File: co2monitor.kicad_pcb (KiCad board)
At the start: 2 copper layers, 70 x 70 mm, 37 parts, among them J1 USB_C_Receptacle_USB2.0, J2 UART, SW1 RESET, SW2 BOOT, U1 AP2112K-3.3, U2 ESP32-S3-WROOM-1, U3 BME680, U4 SCD40, U5 74AHCT1G125, U6 SHT30-DIS

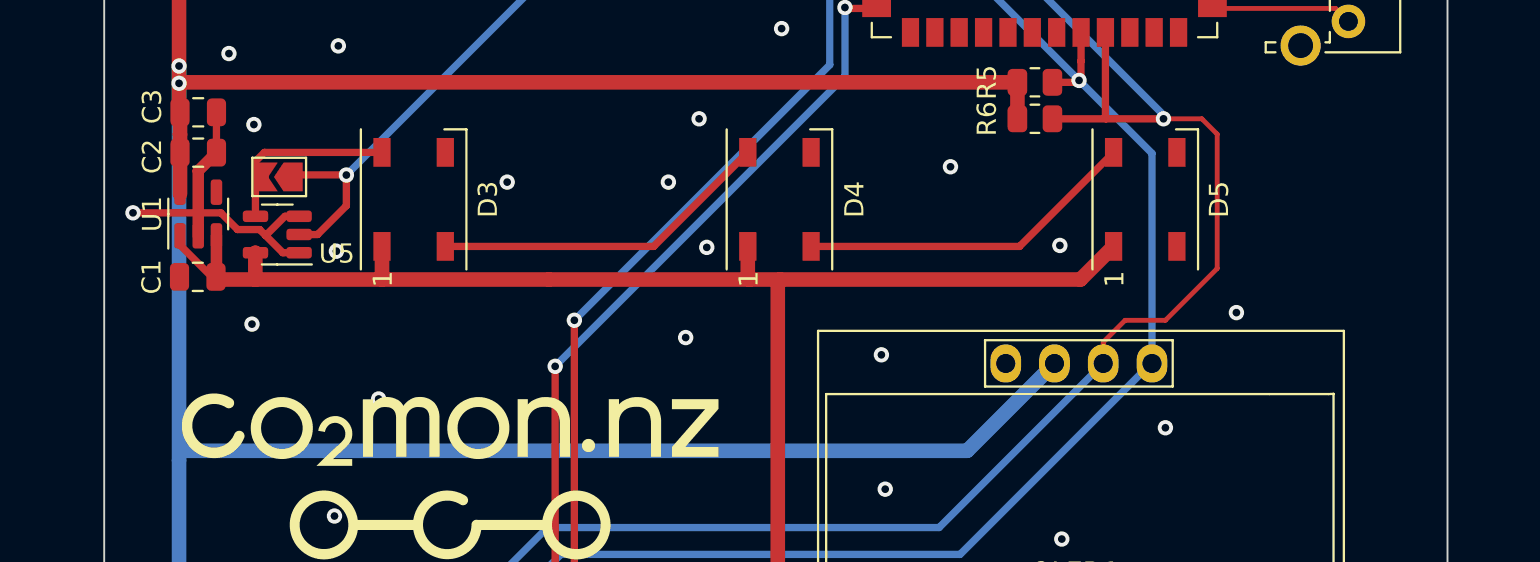
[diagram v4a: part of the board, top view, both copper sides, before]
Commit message: Break out various signals to debugging headers
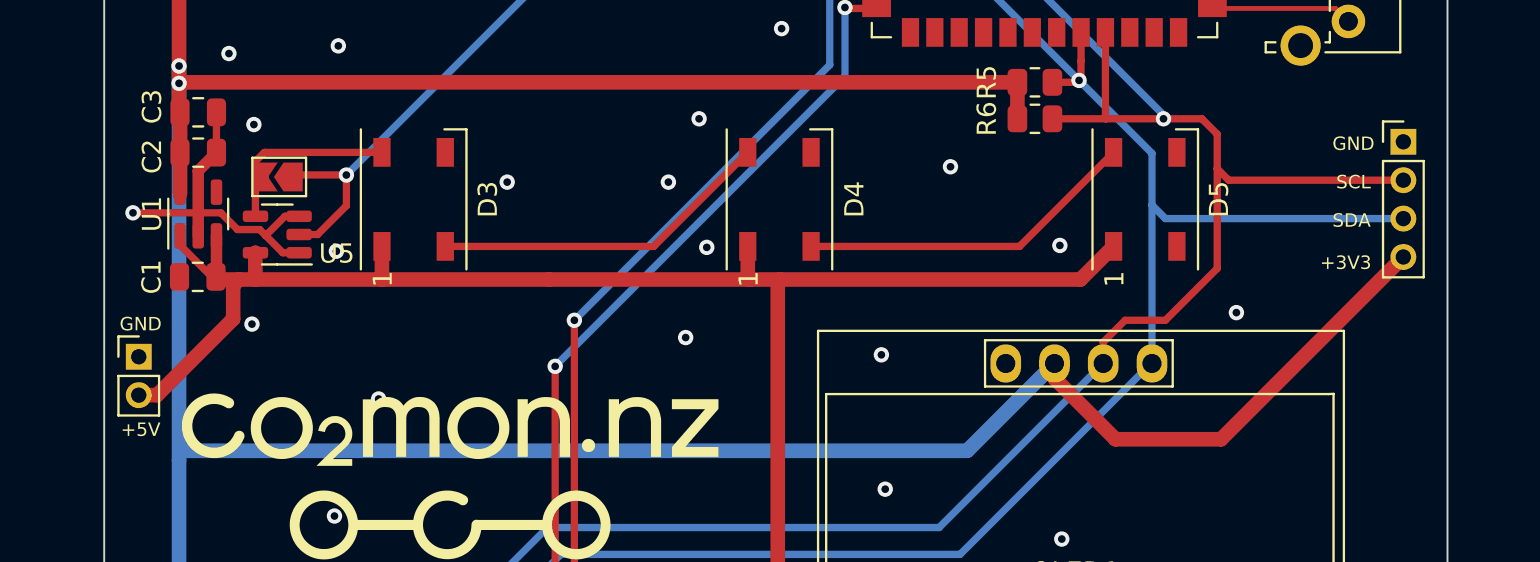
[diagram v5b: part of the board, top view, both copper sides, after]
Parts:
- added J3: I2C, Connector_PinHeader_2.00mm:PinHeader_1x04_P2.00mm_Vertical, F.Cu at (167.7, 102.0)
- added J4: 5V, Connector_PinHeader_2.00mm:PinHeader_1x02_P2.00mm_Vertical, F.Cu at (101.8, 113.2)
- D3, D4, D5: value NeoPixel_THT -> WS2812B
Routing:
- net +3V3: track 226.5 -> 250.7 mm
- net /SDA: track 130.0 -> 143.4 mm
- net /SCL: track 142.1 -> 152.1 mm
- net +5V: track 74.1 -> 82.8 mm
- net GND: vias 35 -> 34
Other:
- board text added: "+3V3"
- board text added: "+5V"
- board text added: "GND"
- board text added: "SCL"
- board text added: "SDA"

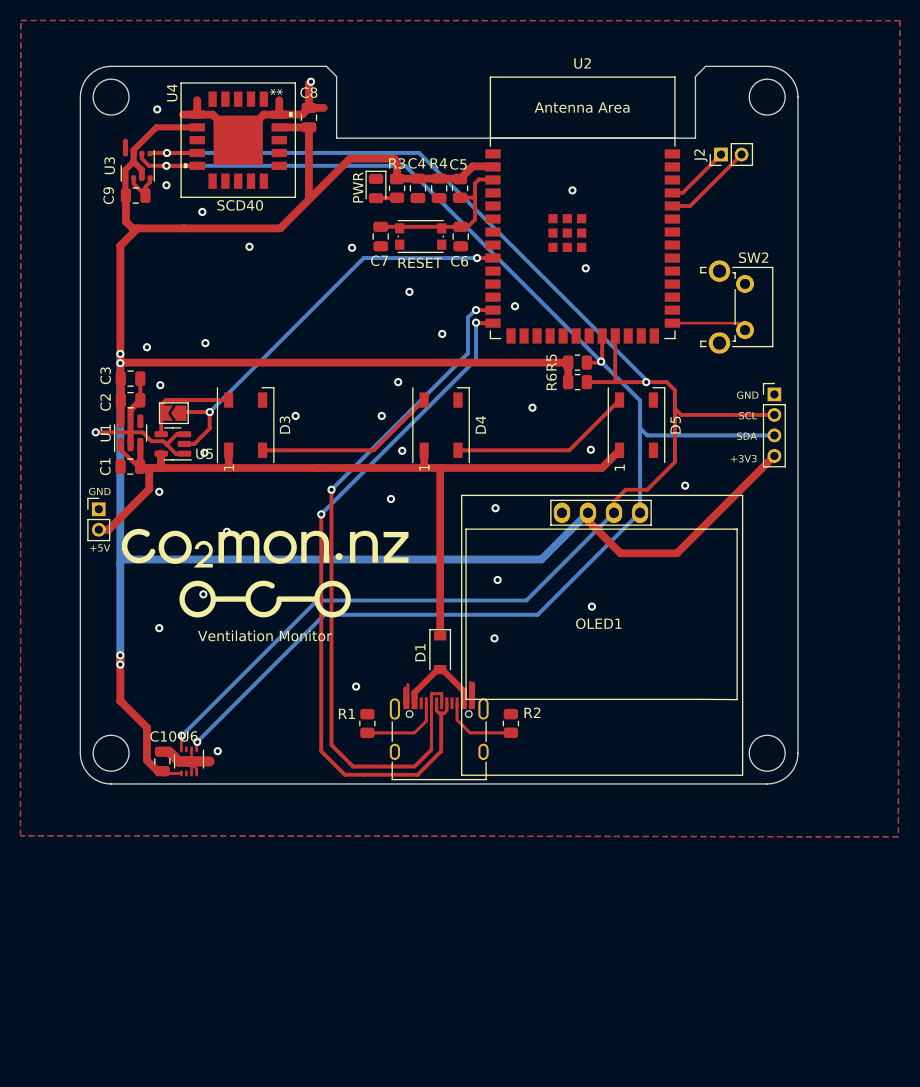
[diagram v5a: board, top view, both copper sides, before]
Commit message: Flip the screen for better positioning.
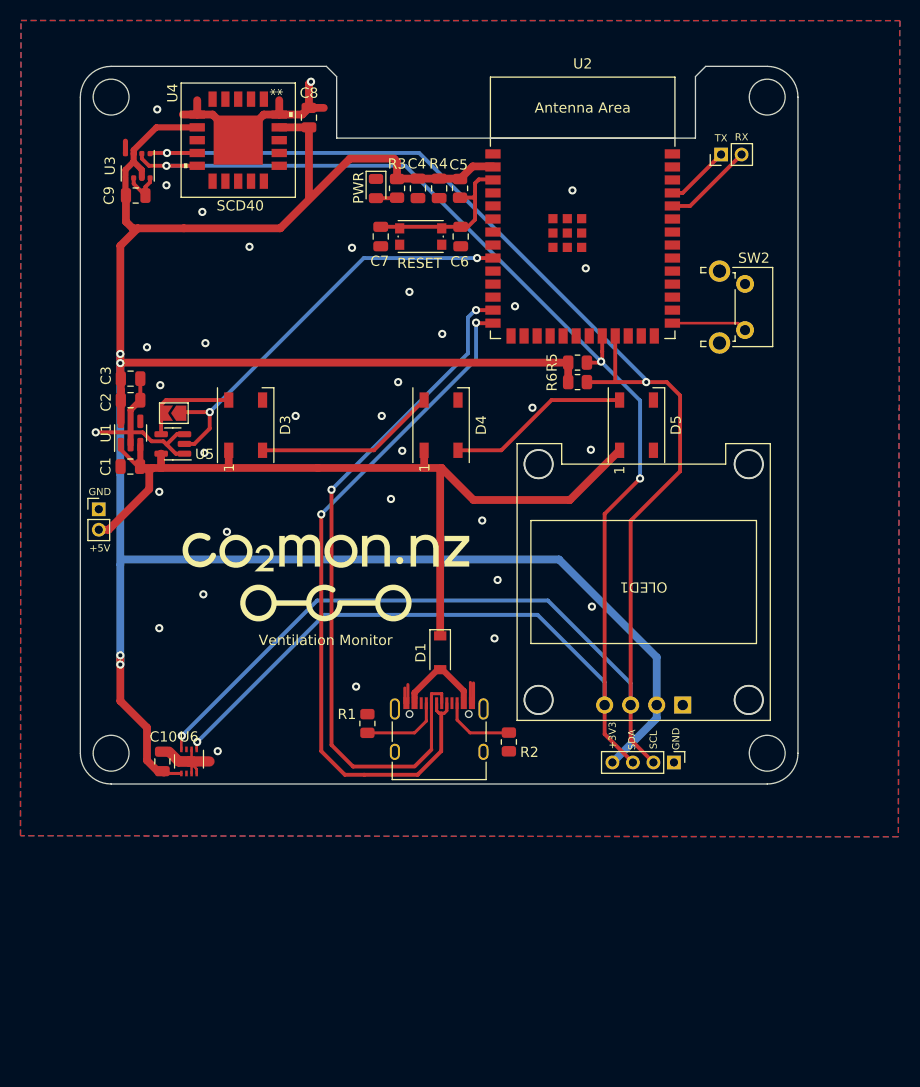
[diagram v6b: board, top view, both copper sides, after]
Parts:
- added H5: MountingHole, MountingHole:MountingHole_2.7mm, F.Cu at (144.7, 108.8)
- added H6: MountingHole, MountingHole:MountingHole_2.7mm, F.Cu at (165.2, 108.8)
- added H7: MountingHole, MountingHole:MountingHole_2.7mm, F.Cu at (144.7, 131.8)
- added H8: MountingHole, MountingHole:MountingHole_2.7mm, F.Cu at (165.2, 131.8)
- OLED1: footprint SSD1306:128x64OLED -> SSD1306-2:OLED_128x64_0.96_small
- moved J3 37.2 mm to (157.9, 137.9), turned to -90 degrees
- moved OLED1 5.81 mm to (154.9, 120.3), turned to 180 degrees
- moved R2 1.81 mm to (141.8, 135.9), turned to -90 degrees
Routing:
- net /SCL: track 152.1 -> 169.5 mm
- net /SDA: track 143.4 -> 154.3 mm, vias 3 -> 4
- net +3V3: track 250.7 -> 247.4 mm
- net +5V: track 82.8 -> 85.4 mm
- net GND: vias 34 -> 33
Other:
- board text added: "RX"
- board text added: "TX"

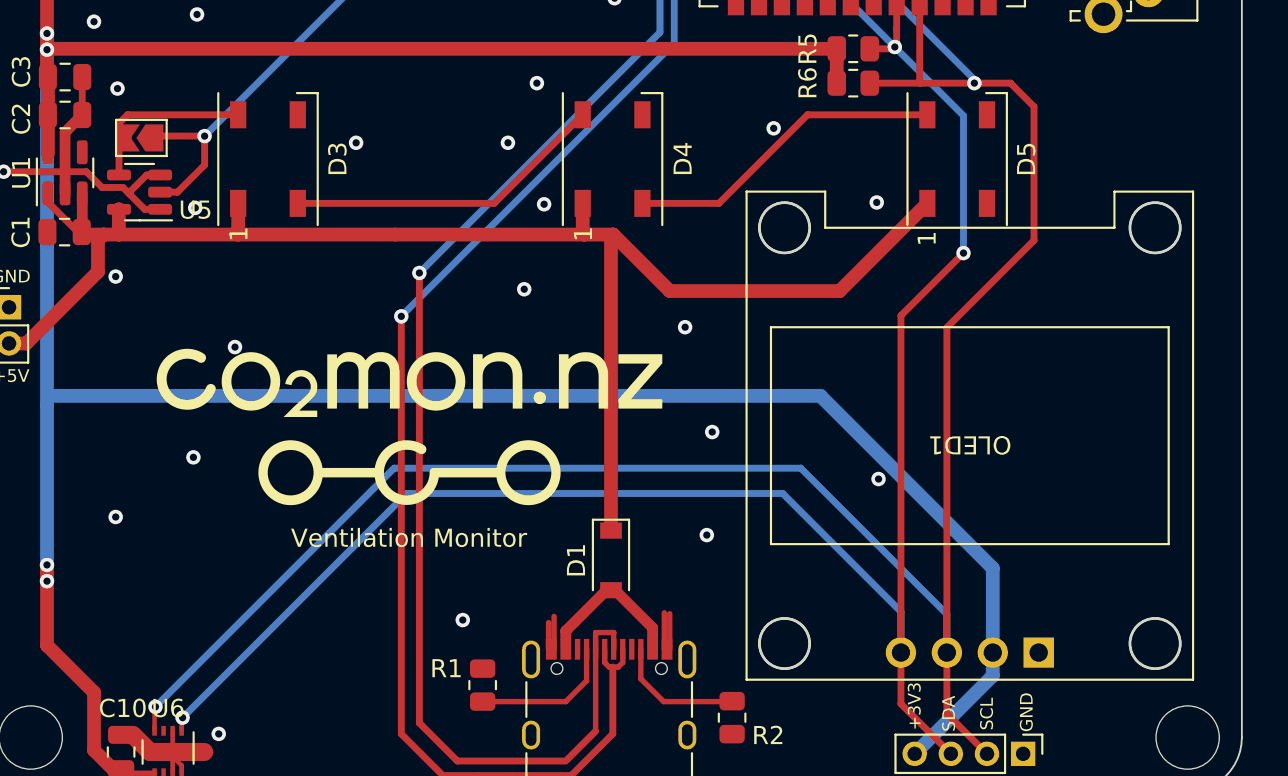
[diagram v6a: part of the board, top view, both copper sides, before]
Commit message: use the mounting holes in the footprint
We don't need to duplicate these ourselves!
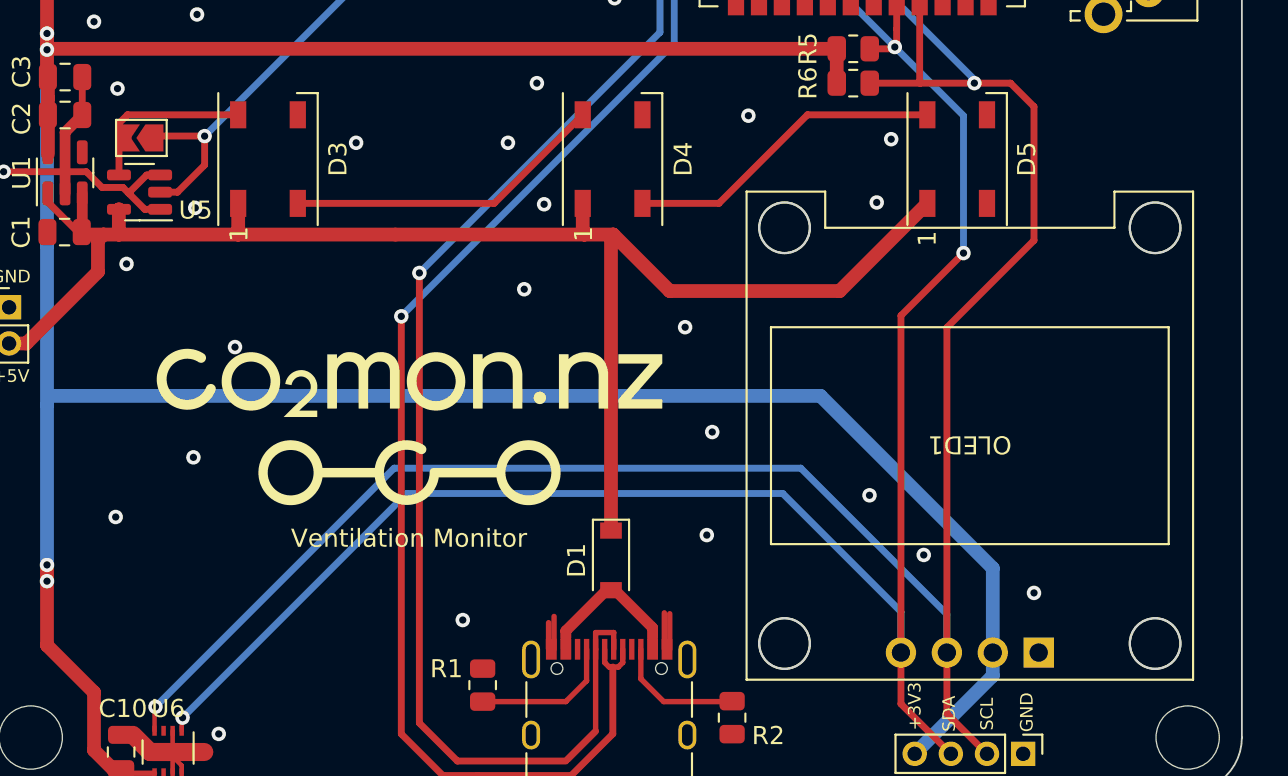
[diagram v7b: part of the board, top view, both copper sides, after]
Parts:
- removed H5, H6, H7, H8: MountingHole, MountingHole:MountingHole_2.7mm
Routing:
- net GND: vias 33 -> 36

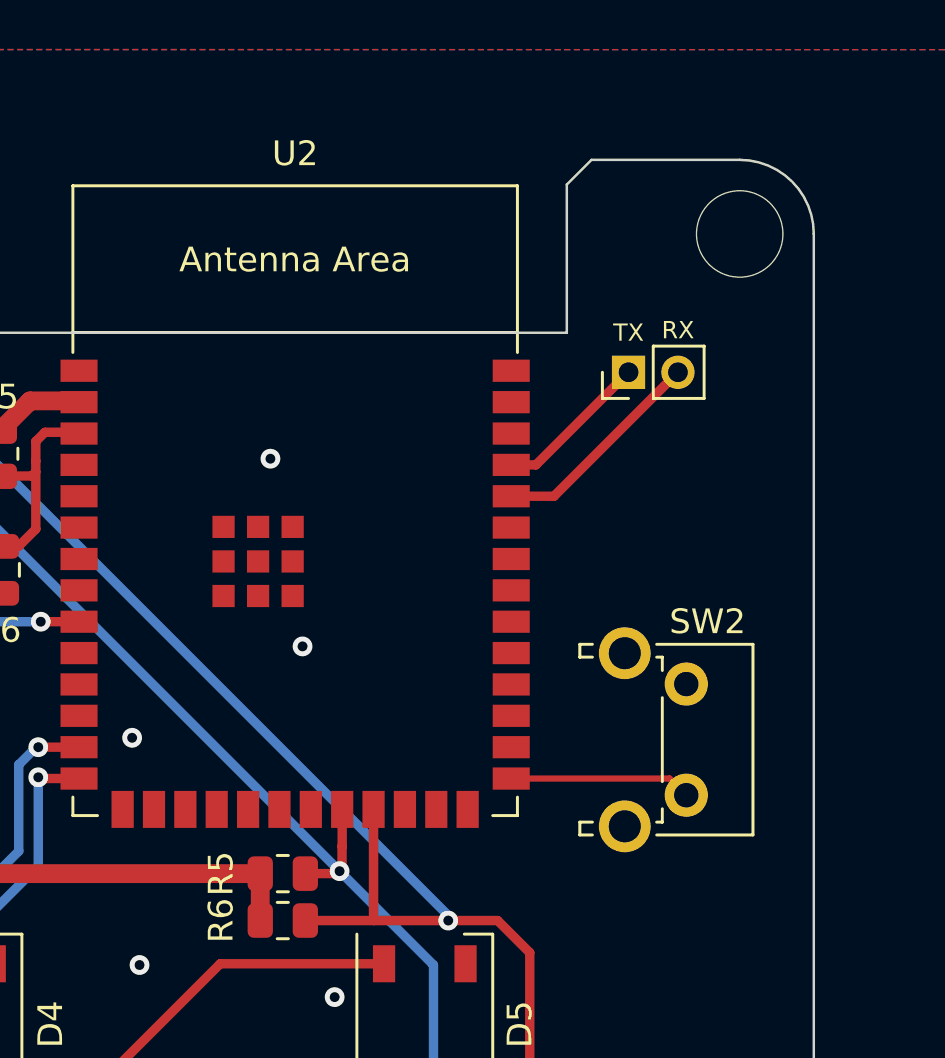
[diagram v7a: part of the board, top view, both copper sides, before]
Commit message: Add JTAG header
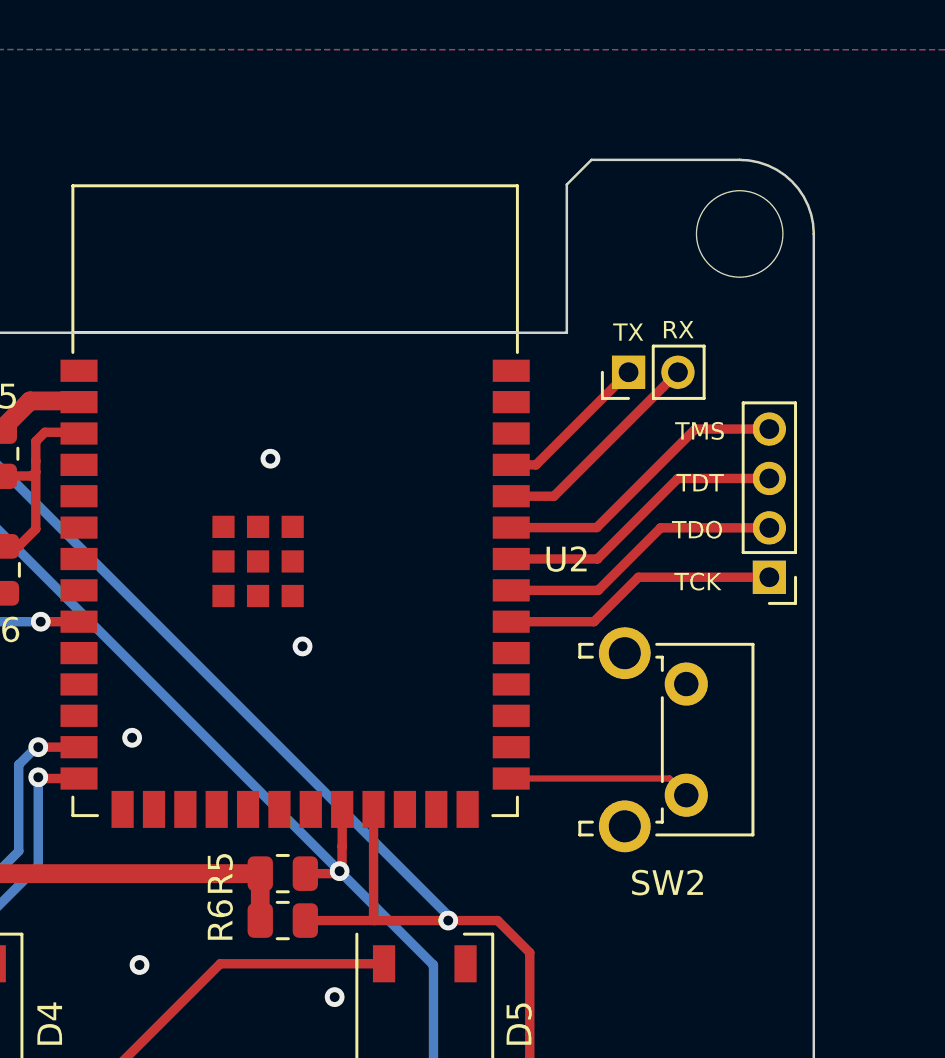
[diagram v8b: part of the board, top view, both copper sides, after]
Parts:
- added J5: JTAG, Connector_PinHeader_2.00mm:PinHeader_1x04_P2.00mm_Vertical, F.Cu at (168.2, 86.9)
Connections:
- U2 pad 32: unconnected-(U2-Pad32) -> /TCK
- U2 pad 33: unconnected-(U2-Pad33) -> /TDO
- U2 pad 34: unconnected-(U2-Pad34) -> /TDI
- U2 pad 35: unconnected-(U2-Pad35) -> /TMS
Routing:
- net /TMS: track 0.00 -> 12.1 mm
- net /TDI: track 0.00 -> 11.8 mm
- net /TDO: track 0.00 -> 11.5 mm
- net /TCK: track 0.00 -> 11.2 mm
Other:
- board text added: "TCK"
- board text added: "TDO"
- board text added: "TDT"
- board text added: "TMS"
